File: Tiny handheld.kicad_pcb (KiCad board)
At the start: 2 copper layers, 34.3 x 58.4 mm, 38 parts, among them J1 Conn_01x04_Female, J3 TYPE-C-31-M-12, U1 ATtiny85-20P, U2 ATtiny85-20M, U3 EEPROM-I2CEIAJ

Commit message: continued wiring
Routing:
- net Net-(D2-Pad1): track 0.00 -> 113.0 mm, vias 0 -> 1
- net Net-(BT1-Pad+): track 0.00 -> 71.7 mm, vias 0 -> 3
- net PB4: track 0.00 -> 65.6 mm, vias 0 -> 1
- net Net-(R1-Pad2): track 0.00 -> 55.7 mm, vias 0 -> 1
- net PB2/SCL/SCK: track 0.00 -> 45.8 mm
- net Net-(D3-Pad1): track 0.00 -> 45.3 mm, vias 0 -> 6
- net PB0/SDA/MOSI: track 0.00 -> 44.9 mm
- net Net-(J3-PadA5): track 0.00 -> 43.9 mm, vias 0 -> 1
- net Net-(R4-Pad2): track 0.00 -> 38.8 mm, vias 0 -> 1
- net (no net): track 0.00 -> 36.6 mm, vias 2 -> 4
- net Net-(R7-Pad2): track 0.00 -> 35.3 mm, vias 0 -> 1
- net Net-(J3-PadB5): track 0.00 -> 34.7 mm, vias 0 -> 1
- net Net-(JP1-Pad1): track 8.92 -> 38.4 mm, vias 0 -> 2
- net Net-(R3-Pad2): track 0.00 -> 24.6 mm, vias 0 -> 1
- net Net-(D1-Pad2): track 0.00 -> 22.1 mm, vias 0 -> 1
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- added copper zone on B.Cu, net GND

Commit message: more connections made
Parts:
- removed BT1: BATTERY-6.8MM_SMD, Snapeda:BAT_BU2032-1
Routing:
- net VCC: track 10.7 -> 186.9 mm, vias 0 -> 12
- net ExtVCC: track 21.6 -> 94.3 mm, vias 5 -> 6
- net GND: track 11.9 -> 72.5 mm, vias 1 -> 10
- net PB3: track 19.5 -> 66.4 mm, vias 0 -> 3
- net Net-(C1-Pad2): track 7.06 -> 26.5 mm, vias 2 -> 5
- net PB0/SDA/MOSI: track 44.9 -> 59.7 mm
- net Net-(JP1-Pad3): track 19.5 -> 29.7 mm, vias 0 -> 3
- net PB5/RES: track 13.0 -> 21.3 mm, vias 2 -> 3
- net Net-(R7-Pad2): track 35.3 -> 36.8 mm
- net Net-(J3-PadA5): track 43.9 -> 45.3 mm
- net Net-(JP1-Pad1): track 38.4 -> 39.5 mm
- net Net-(R3-Pad2): track 24.6 -> 25.5 mm
- net PB1/MISO: track 42.0 -> 42.8 mm
- net PB2/SCL/SCK: track 45.8 -> 46.5 mm
- added copper zone on F.Cu, net GND

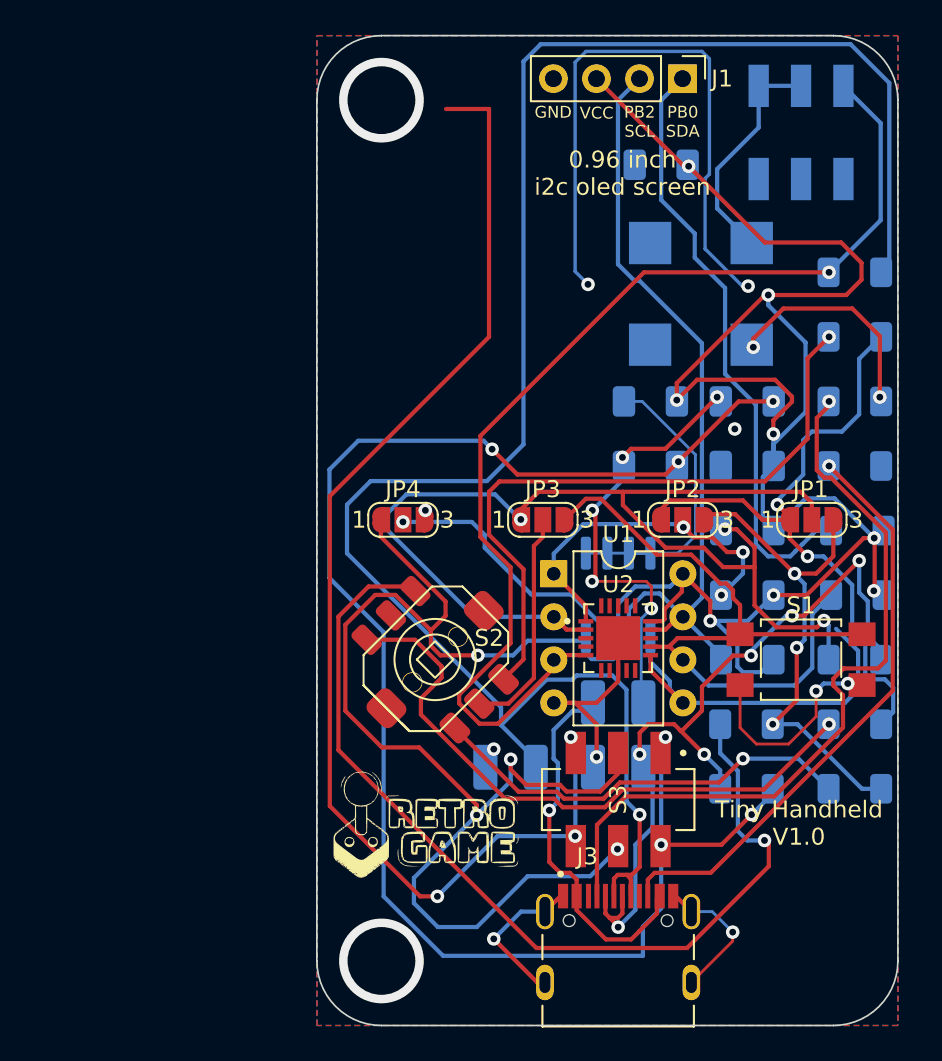
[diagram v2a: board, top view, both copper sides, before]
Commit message: all errors (that i found critical) resolved
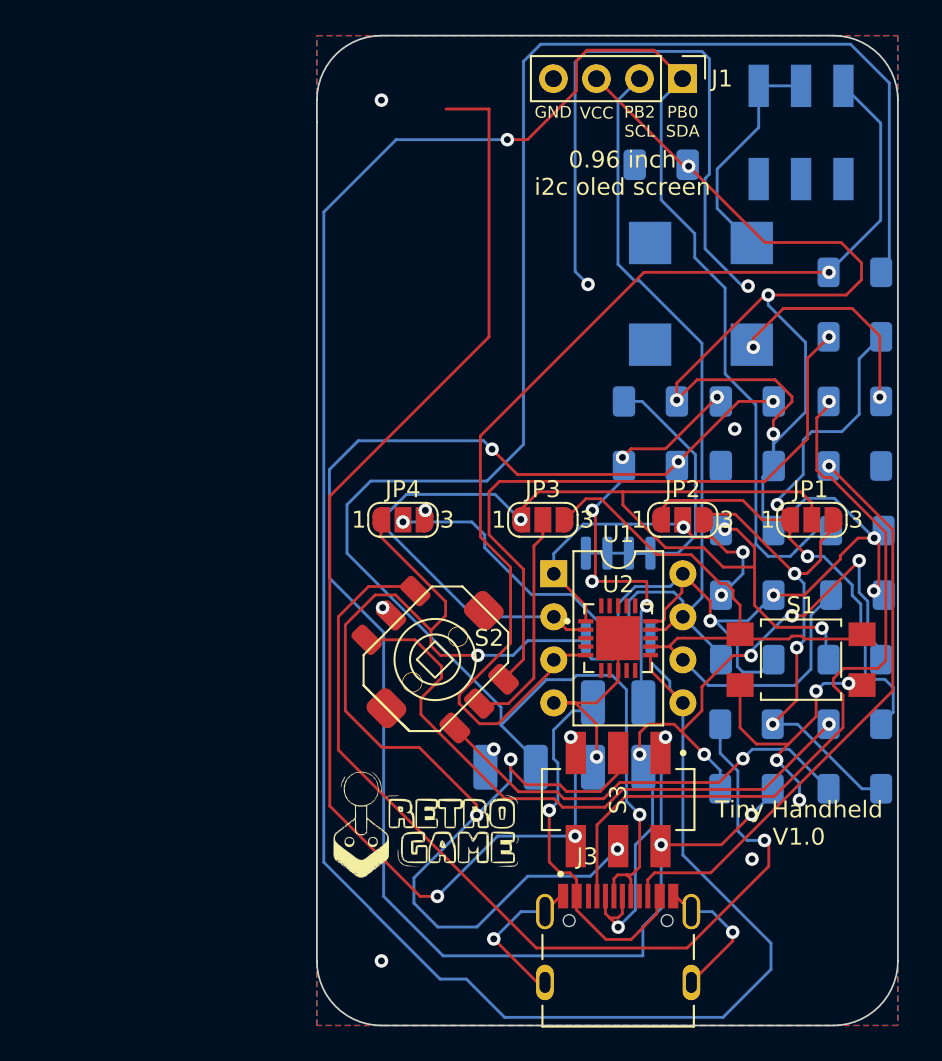
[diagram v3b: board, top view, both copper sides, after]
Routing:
- net PB0/SDA/MOSI: track 59.7 -> 159.4 mm, vias 0 -> 1
- net GND: track 72.5 -> 76.8 mm, vias 10 -> 14
- net PB2/SCL/SCK: track 46.5 -> 47.3 mm
- net PB3: track 66.4 -> 65.8 mm

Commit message: board cleanup
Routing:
- net Net-(BT1-Pad+): track 71.7 -> 5.96 mm, vias 3 -> 2
- net (no net): track 36.6 -> 0.00 mm, vias 4 -> 0
- net PB0/SDA/MOSI: track 159.4 -> 157.5 mm
- net Net-(D3-Pad1): track 45.1 -> 43.7 mm
- net PB1/MISO: track 43.2 -> 42.1 mm
- net Net-(D2-Pad1): track 112.9 -> 111.8 mm
- net Net-(JP1-Pad3): track 29.3 -> 28.4 mm
- net PB5/RES: track 21.3 -> 20.4 mm, vias 3 -> 2
- net Net-(D1-Pad2): track 22.1 -> 21.2 mm
- net PB4: track 65.5 -> 64.6 mm
- net PB3: track 65.8 -> 64.9 mm
- net Net-(JP1-Pad1): track 39.5 -> 38.8 mm
- net PB2/SCL/SCK: track 47.3 -> 46.8 mm
- net VCC: track 187.2 -> 186.7 mm
- net Net-(C1-Pad2): track 26.1 -> 25.7 mm, vias 5 -> 4

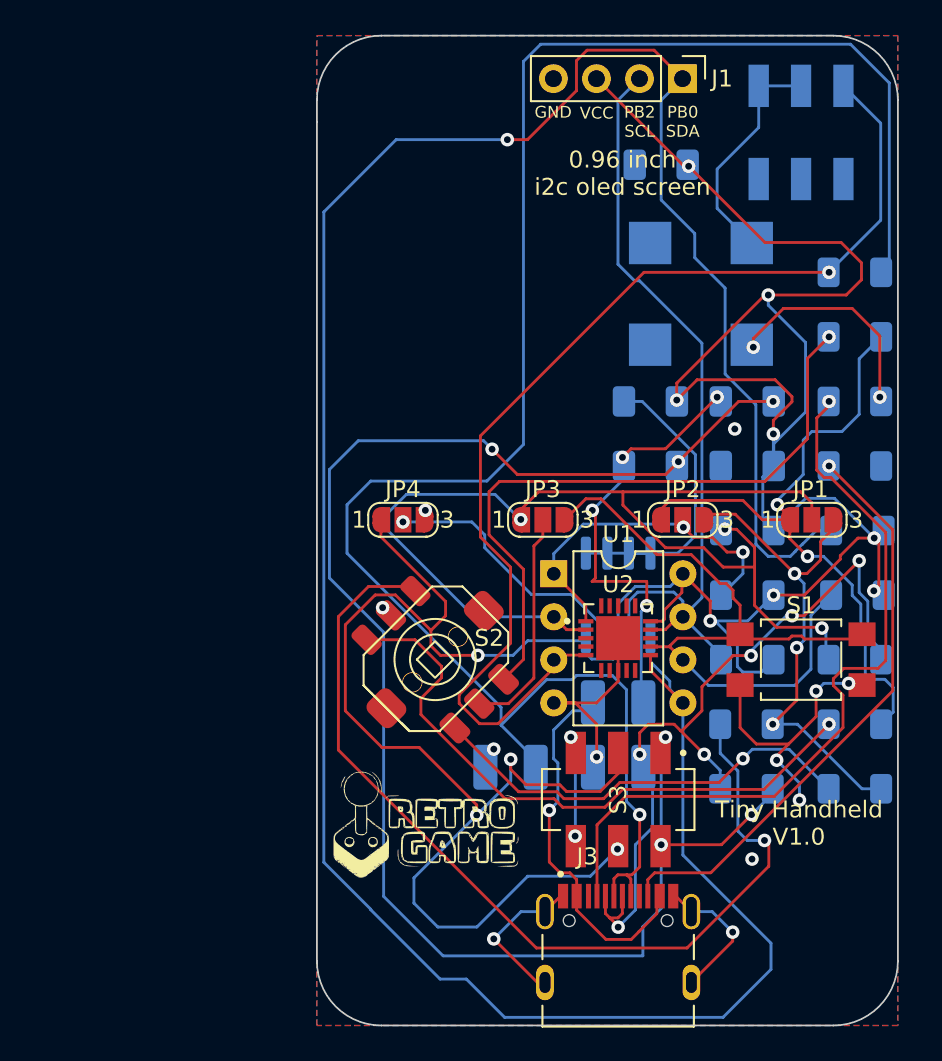
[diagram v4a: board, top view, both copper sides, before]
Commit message: first melted circuit tryout (rounded tracks)
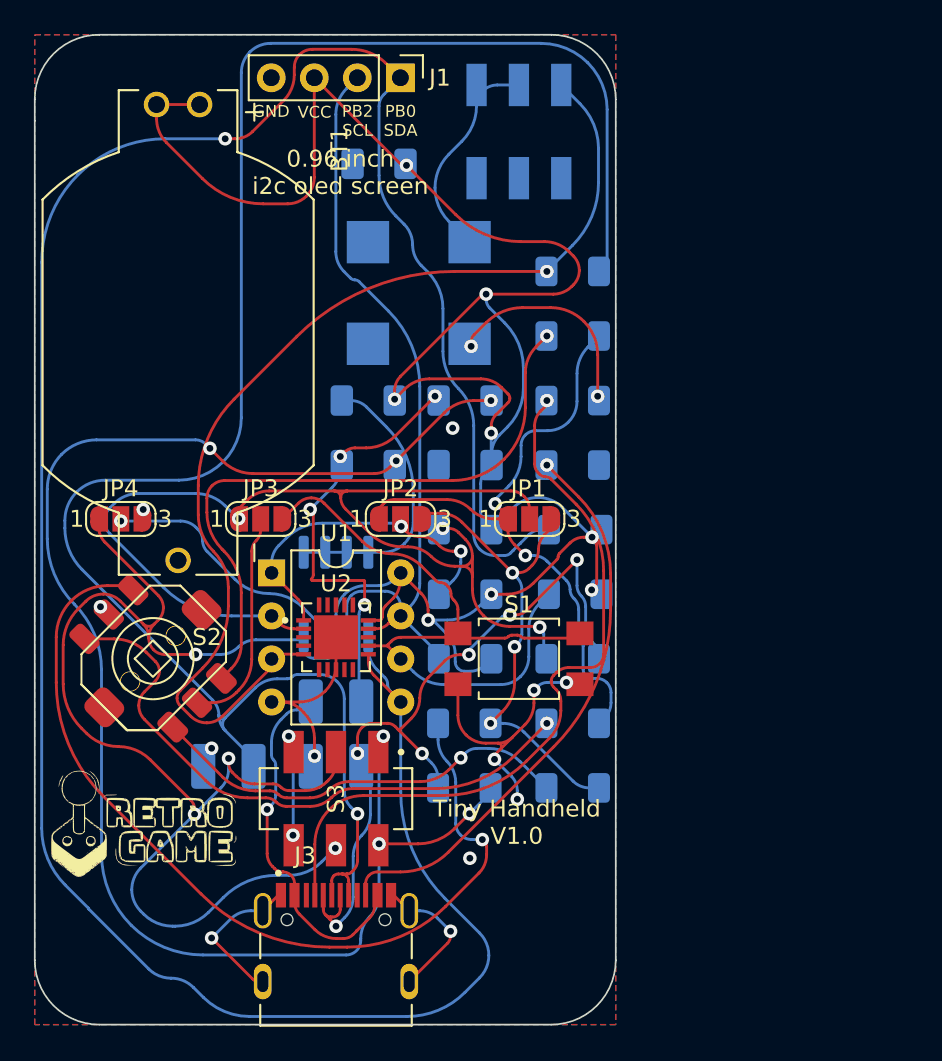
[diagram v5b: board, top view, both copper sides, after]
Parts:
- added BT1: BATTERY-6.8MM_SMD, Snapeda:BAT_BU2032-1, F.Cu at (141.7, 89.9)
- moved C5 16.7 mm to (153.5, 80.0)
- moved G*** 16.7 mm to (139.6, 119.0)
- moved R10 16.7 mm to (165.1, 105.4)
- moved R12 16.7 mm to (165.1, 101.5)
- moved R13 16.7 mm to (165.0, 97.7)
- moved R14 16.7 mm to (165.0, 93.9)
- moved R3 16.7 mm to (165.0, 116.8)
- moved R4 16.7 mm to (165.0, 90.1)
- moved R7 16.7 mm to (165.0, 113.0)
- moved R8 16.7 mm to (165.0, 109.2)
- moved R9 16.7 mm to (165.0, 86.3)
- moved S1 16.7 mm to (161.8, 109.2)
- moved S4 16.7 mm to (161.8, 78.1)
- moved U1 16.7 mm to (147.2, 104.1)
- moved C1 16.7 mm to (152.9, 97.7)
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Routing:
- net VCC: track 186.7 -> 204.1 mm
- net PB0/SDA/MOSI: track 157.5 -> 153.7 mm
- net ExtVCC: track 94.1 -> 91.6 mm
- net GND: track 76.4 -> 74.2 mm
- net PB4: track 64.6 -> 62.5 mm
- net Net-(R1-Pad2): track 55.3 -> 53.3 mm
- net Net-(JP1-Pad1): track 38.8 -> 37.3 mm
- net Net-(J3-PadA5): track 45.3 -> 43.9 mm
- net Net-(J3-PadB5): track 34.9 -> 33.8 mm
- net Net-(R7-Pad2): track 36.8 -> 35.7 mm
- net Net-(R4-Pad2): track 39.0 -> 38.0 mm
- net Net-(LS1-PadP): track 13.6 -> 12.6 mm
- net PB1/MISO: track 42.1 -> 41.2 mm
- net PB2/SCL/SCK: track 46.8 -> 46.0 mm
- net Net-(D2-Pad1): track 111.8 -> 110.9 mm
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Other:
- board text removed: "+"

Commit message: removed fluid traces, First functional design
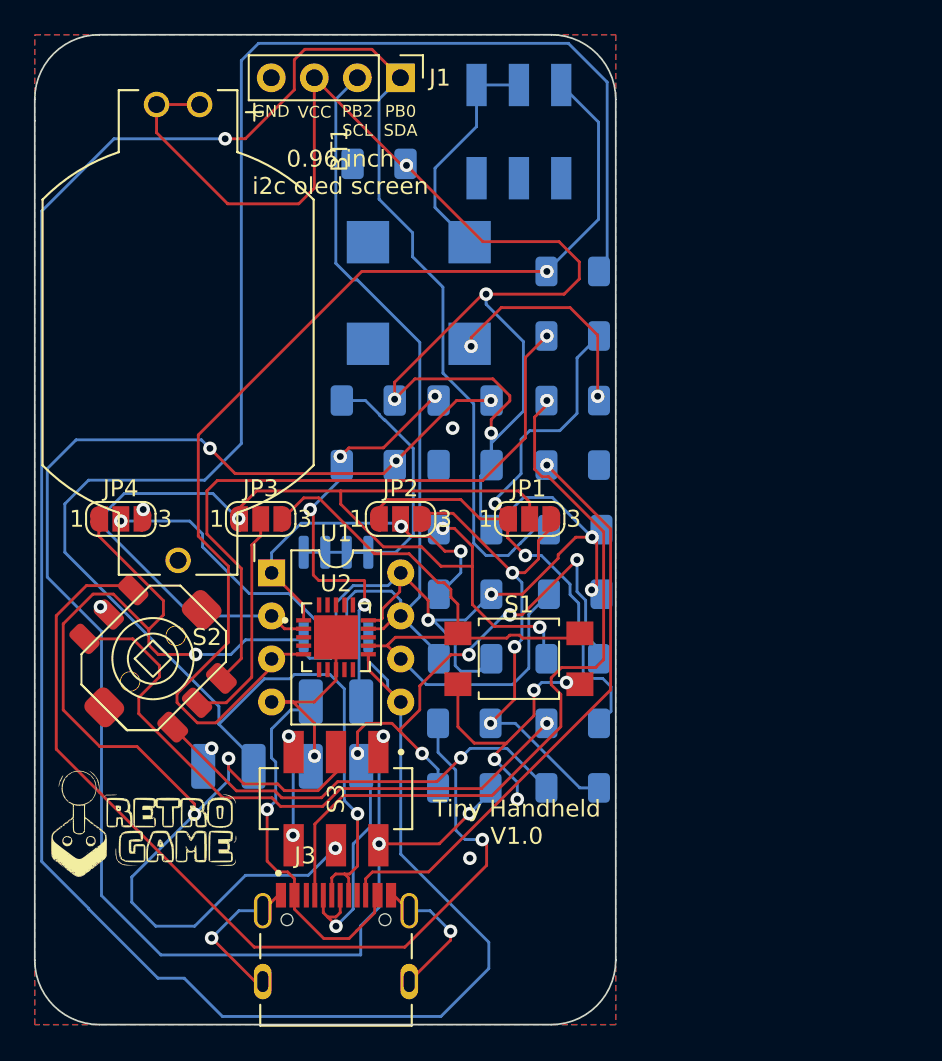
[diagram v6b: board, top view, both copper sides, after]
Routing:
- net VCC: track 204.1 -> 208.9 mm
- net PB0/SDA/MOSI: track 153.7 -> 157.5 mm
- net ExtVCC: track 91.6 -> 94.1 mm
- net GND: track 74.2 -> 76.6 mm
- net PB4: track 62.5 -> 64.6 mm
- net Net-(R1-Pad2): track 53.3 -> 55.3 mm
- net Net-(JP1-Pad1): track 37.3 -> 38.8 mm
- net Net-(J3-PadA5): track 43.9 -> 45.3 mm
- net Net-(J3-PadB5): track 33.8 -> 34.9 mm
- net Net-(R7-Pad2): track 35.7 -> 36.8 mm
- net Net-(R4-Pad2): track 38.0 -> 39.0 mm
- net Net-(LS1-PadP): track 12.6 -> 13.6 mm
- net PB1/MISO: track 41.2 -> 42.1 mm
- net PB2/SCL/SCK: track 46.0 -> 46.8 mm
- net Net-(D2-Pad1): track 110.9 -> 111.8 mm
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
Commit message: V1.0
Added silkscreen and finished up with straight lines (no curves yet)
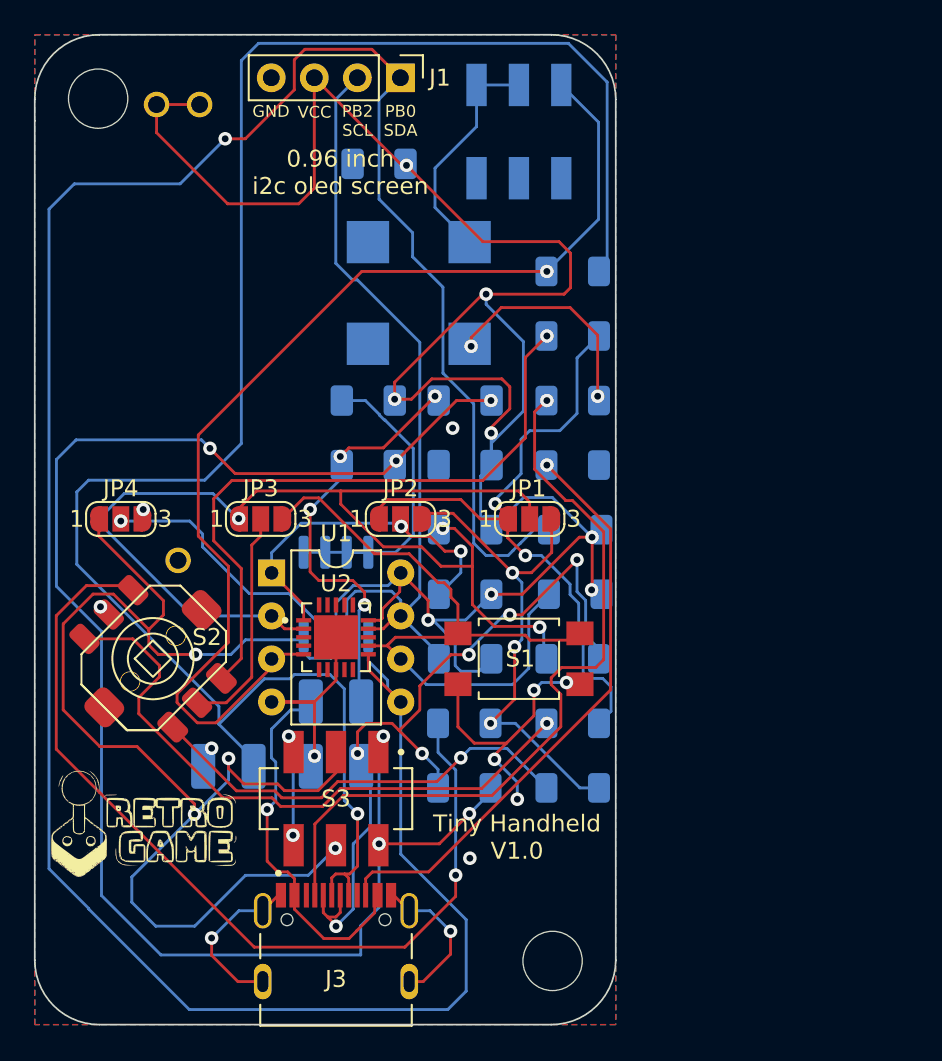
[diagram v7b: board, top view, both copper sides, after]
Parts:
- added REF**: MountingHole_3.5mm, MountingHole:MountingHole_3.5mm, F.Cu at (136.9, 76.1)
- added REF**: MountingHole_3.5mm, MountingHole:MountingHole_3.5mm, F.Cu at (163.8, 127.0)
- added REF**: OSHW-Logo2_7.3x6mm_SilkScreen, Symbol:OSHW-Logo2_7.3x6mm_SilkScreen, B.Cu at (163.5, 122.0)
- added REF**: KiCad-Logo2_5mm_SilkScreen, Symbol:KiCad-Logo2_5mm_SilkScreen, B.Cu at (136.7, 118.8)
- BT1: moved to B.Cu
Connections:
- BT1 pad : VCC -> (no net)
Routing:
- net Net-(R1-Pad2): track 55.3 -> 53.2 mm
- net PB0/SDA/MOSI: track 157.5 -> 155.5 mm
- net GND: track 76.6 -> 78.5 mm
- net PB4: track 64.6 -> 65.5 mm
- net Net-(R4-Pad2): track 39.0 -> 38.2 mm
- net Net-(D2-Pad1): track 111.8 -> 111.2 mm
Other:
- board text added: "+"
- board text added: "-"

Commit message: Added curvy wires
Because they are the best thing in this straight world
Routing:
- net VCC: track 208.4 -> 201.9 mm
- net PB0/SDA/MOSI: track 155.5 -> 153.8 mm
- net Net-(JP1-Pad1): track 38.8 -> 37.5 mm
- net ExtVCC: track 93.6 -> 92.5 mm
- net PB3: track 64.9 -> 65.8 mm
- net PB4: track 65.5 -> 64.8 mm
- net Net-(J3-PadA5): track 45.3 -> 44.6 mm
- net PB1/MISO: track 42.2 -> 41.5 mm
- net GND: track 78.5 -> 77.8 mm
- net Net-(R7-Pad2): track 36.8 -> 36.2 mm
- net Net-(D1-Pad2): track 21.2 -> 20.7 mm
- net Net-(R1-Pad2): track 53.2 -> 52.7 mm
- net Net-(R4-Pad2): track 38.2 -> 37.7 mm
